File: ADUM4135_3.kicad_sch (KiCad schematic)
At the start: 37 parts, among them Q10 MJD45H11T4G, Q11 MJD44H11T4G, Q12 MJD45H11T4G, Q9 MJD44H11T4G

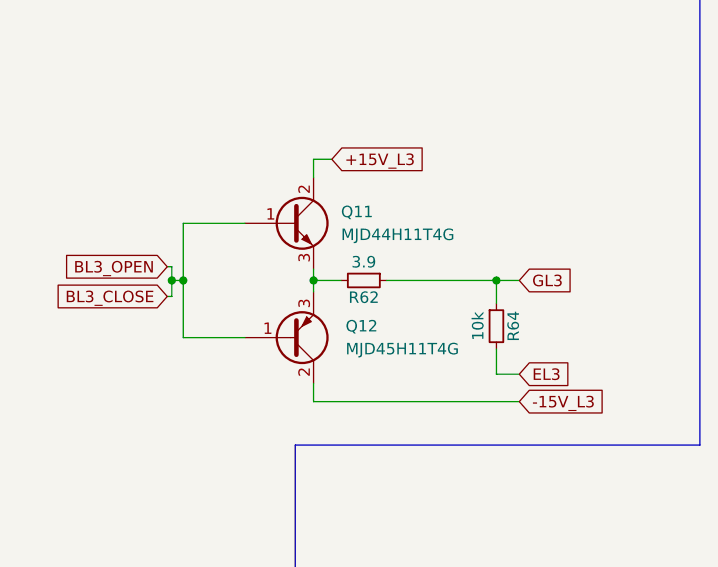
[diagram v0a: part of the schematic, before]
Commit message: REV2.1 - добавил конденсатор по питанию измерения DC
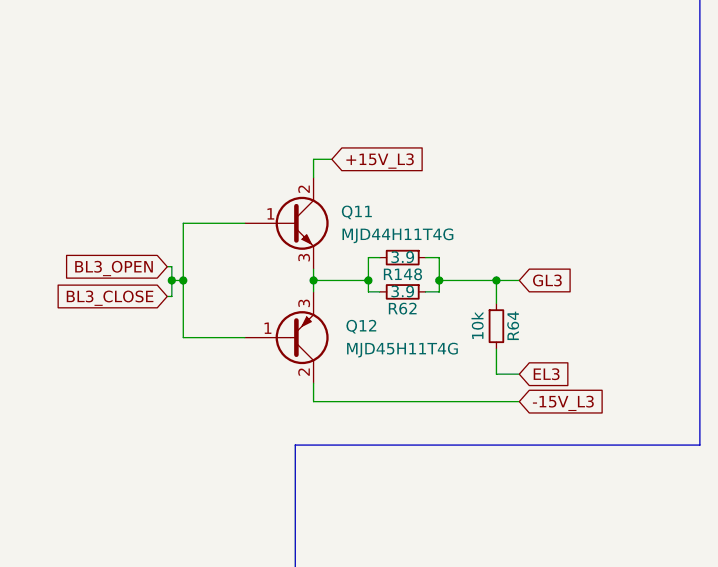
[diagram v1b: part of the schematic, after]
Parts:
- added R148: 3.9, Resistor_SMD:R_2512_6332Metric_Pad1.40x3.35mm_HandSolder, symbol Device:R_Small
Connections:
- net GL3: now also R148.1
- net at Q11.3 (E), Q12.3 (E), R62.2: now also R148.2
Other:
- moved on the sheet: R62
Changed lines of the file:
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@@
   (junction (at 151.892 54.864) (diameter 0) (color 0 0 0 0)
   )
+  (junction (at 173.736 141.478) (diameter 0) (color 0 0 0 0)
+  )
+  (junction (at 179.832 141.478) (diameter 0) (color 0 0 0 0)
+  )
   (junction (at 183.896 54.864) (diameter 0) (color 0 0 0 0)
   )
@@
   (junction (at 126.238 155.448) (diameter 0) (color 0 0 0 0)
   )
-  (junction (at 173.736 141.478) (diameter 0) (color 0 0 0 0)
+  (junction (at 194.056 141.478) (diameter 0) (color 0 0 0 0)
   )
   (junction (at 189.992 54.864) (diameter 0) (color 0 0 0 0)
@@
   (junction (at 117.602 61.722) (diameter 0) (color 0 0 0 0)
   )
-  (junction (at 194.056 141.478) (diameter 0) (color 0 0 0 0)
-  )
   (junction (at 112.522 61.722) (diameter 0) (color 0 0 0 0)
   )
@@
   )
   (junction (at 109.982 155.448) (diameter 0) (color 0 0 0 0)
+  )
+  (junction (at 187.706 141.478) (diameter 0) (color 0 0 0 0)
   )
   (junction (at 167.64 54.864) (diameter 0) (color 0 0 0 0)
@@
     (stroke (width 0) (type default) (color 0 0 0 0))
   )
+  (wire (pts (xy 179.832 138.938) (xy 179.832 141.478))
+    (stroke (width 0) (type default) (color 0 0 0 0))
+  )
   (wire (pts (xy 151.384 53.34) (xy 151.892 53.34))
     (stroke (width 0) (type default) (color 0 0 0 0))
@@
     (stroke (width 0) (type default) (color 0 0 0 0))
   )
-  (wire (pts (xy 173.736 141.478) (xy 176.784 141.478))
-    (stroke (width 0) (type default) (color 0 0 0 0))
-  )
   (wire (pts (xy 177.546 52.578) (xy 176.53 52.578))
     (stroke (width 0) (type default) (color 0 0 0 0))
   )
+  (wire (pts (xy 173.736 141.478) (xy 173.736 142.748))
+    (stroke (width 0) (type default) (color 0 0 0 0))
+  )
   (wire (pts (xy 167.64 53.594) (xy 167.64 54.864))
     (stroke (width 0) (type default) (color 0 0 0 0))
   )
+  (wire (pts (xy 173.736 141.478) (xy 179.832 141.478))
+    (stroke (width 0) (type default) (color 0 0 0 0))
+  )
   (wire (pts (xy 109.982 155.448) (xy 109.982 146.812))
     (stroke (width 0) (type default) (color 0 0 0 0))
@@
     (stroke (width 0) (type default) (color 0 0 0 0))
   )
-  (wire (pts (xy 173.736 141.478) (xy 173.736 142.748))
-    (stroke (width 0) (type default) (color 0 0 0 0))
-  )
   (wire (pts (xy 151.892 53.34) (xy 151.892 54.864))
     (stroke (width 0) (type default) (color 0 0 0 0))
   )
+  (wire (pts (xy 181.102 138.938) (xy 179.832 138.938))
+    (stroke (width 0) (type default) (color 0 0 0 0))
+  )
   (polyline (pts (xy 142.24 104.14) (xy 216.662 104.14))
     (stroke (width 0) (type default) (color 0 0 0 0))
@@
     (stroke (width 0) (type default) (color 0 0 0 0))
   )
-  (wire (pts (xy 181.864 141.478) (xy 194.056 141.478))
-    (stroke (width 0) (type default) (color 0 0 0 0))
-  )
   (wire (pts (xy 123.19 139.954) (xy 125.984 139.954))
     (stroke (width 0) (type default) (color 0 0 0 0))
@@
     (stroke (width 0) (type default) (color 0 0 0 0))
   )
+  (wire (pts (xy 179.832 142.748) (xy 181.102 142.748))
+    (stroke (width 0) (type default) (color 0 0 0 0))
+  )
   (wire (pts (xy 107.442 81.788) (xy 110.236 81.788))
     (stroke (width 0) (type default) (color 0 0 0 0))
@@
     (stroke (width 0) (type default) (color 0 0 0 0))
   )
+  (wire (pts (xy 187.706 138.938) (xy 187.706 141.478))
+    (stroke (width 0) (type default) (color 0 0 0 0))
+  )
   (wire (pts (xy 167.64 66.294) (xy 167.64 68.326))
     (stroke (width 0) (type default) (color 0 0 0 0))
@@
     (stroke (width 0) (type default) (color 0 0 0 0))
   )
+  (wire (pts (xy 187.706 142.748) (xy 186.182 142.748))
+    (stroke (width 0) (type default) (color 0 0 0 0))
+  )
   (wire (pts (xy 94.996 65.532) (xy 99.06 65.532))
     (stroke (width 0) (type default) (color 0 0 0 0))
@@
     (stroke (width 0) (type default) (color 0 0 0 0))
   )
+  (wire (pts (xy 187.706 141.478) (xy 187.706 142.748))
+    (stroke (width 0) (type default) (color 0 0 0 0))
+  )
   (wire (pts (xy 104.394 71.882) (xy 107.442 71.882))
     (stroke (width 0) (type default) (color 0 0 0 0))
@@
     (stroke (width 0) (type default) (color 0 0 0 0))
   )
+  (wire (pts (xy 179.832 141.478) (xy 179.832 142.748))
+    (stroke (width 0) (type default) (color 0 0 0 0))
+  )
   (wire (pts (xy 151.892 56.642) (xy 151.892 54.864))
     (stroke (width 0) (type default) (color 0 0 0 0))
@@
     (stroke (width 0) (type default) (color 0 0 0 0))
   )
+  (wire (pts (xy 187.706 141.478) (xy 194.056 141.478))
+    (stroke (width 0) (type default) (color 0 0 0 0))
+  )
   (wire (pts (xy 183.896 57.404) (xy 183.896 54.864))
     (stroke (width 0) (type default) (color 0 0 0 0))
@@
   )
   (wire (pts (xy 94.742 150.622) (xy 98.806 150.622))
+    (stroke (width 0) (type default) (color 0 0 0 0))
+  )
+  (wire (pts (xy 186.182 138.938) (xy 187.706 138.938))
     (stroke (width 0) (type default) (color 0 0 0 0))
   )
@@
     (pin "2")
   )
-  (symbol (lib_id "Device:R_Small") (at 179.324 141.478 270) (unit 1)
+  (symbol (lib_id "Device:R_Small") (at 183.642 142.748 270) (unit 1)
     (in_bom yes) (on_board yes)
-    (property "Reference" "R62" (id 0) (at 179.324 143.383 90))
-    (property "Value" "3.9" (id 1) (at 179.324 139.446 90))
-    (property "Footprint" "Resistor_SMD:R_2512_6332Metric_Pad1.40x3.35mm_HandSolder" (id 2) (at 179.324 141.478 0)
-      (effects (font (size 1.27 1.27)) hide)
-    )
-    (property "Datasheet" "~" (id 3) (at 179.324 141.478 0)
-      (effects (font (size 1.27 1.27)) hide)
-    )
+    (property "Reference" "R62" (id 0) (at 183.642 144.653 90))
+    (property "Value" "3.9" (id 1) (at 183.642 142.748 90))
+    (property "Footprint" "Resistor_SMD:R_2512_6332Metric_Pad1.40x3.35mm_HandSolder" (id 2) (at 183.642 142.748 0)
+      (effects (font (size 1.27 1.27)) hide)
+    )
+    (property "Datasheet" "~" (id 3) (at 183.642 142.748 0)
+      (effects (font (size 1.27 1.27)) hide)
+    )
+    (pin "1")
+    (pin "2")
+  )
+  (symbol (lib_id "Device:R_Small") (at 183.642 138.938 270) (unit 1)
+    (in_bom yes) (on_board yes)
+    (property "Reference" "R148" (id 0) (at 183.642 140.843 90))
+    (property "Value" "3.9" (id 1) (at 183.642 138.938 90))
+    (property "Footprint" "Resistor_SMD:R_2512_6332Metric_Pad1.40x3.35mm_HandSolder" (id 2) (at 183.642 138.938 0)
+      (effects (font (size 1.27 1.27)) hide)
+    )
+    (property "Datasheet" "~" (id 3) (at 183.642 138.938 0)
+      (effects (font (size 1.27 1.27)) hide)
+    )

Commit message: Версия для резонита REV2.1
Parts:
- removed R58, R60: 2.2k, Resistor_SMD:R_0805_2012Metric_Pad1.20x1.40mm_HandSolder, symbol Device:R_Small
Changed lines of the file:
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@@
   (junction (at 189.992 54.864) (diameter 0) (color 0 0 0 0)
-  )
-  (junction (at 117.602 61.722) (diameter 0) (color 0 0 0 0)
   )
   (junction (at 112.522 61.722) (diameter 0) (color 0 0 0 0)
@@
     (stroke (width 0) (type default) (color 0 0 0 0))
   )
-  (wire (pts (xy 126.238 70.866) (xy 126.238 61.722))
-    (stroke (width 0) (type default) (color 0 0 0 0))
-  )
   (wire (pts (xy 159.258 135.128) (xy 159.258 141.478))
     (stroke (width 0) (type default) (color 0 0 0 0))
@@
     (stroke (width 0) (type default) (color 0 0 0 0))
   )
-  (wire (pts (xy 113.03 139.954) (xy 118.11 139.954))
-    (stroke (width 0) (type default) (color 0 0 0 0))
-  )
   (wire (pts (xy 183.896 54.864) (xy 189.992 54.864))
     (stroke (width 0) (type default) (color 0 0 0 0))
@@
     (stroke (width 0) (type default) (color 0 0 0 0))
   )
-  (wire (pts (xy 123.19 139.954) (xy 125.984 139.954))
-    (stroke (width 0) (type default) (color 0 0 0 0))
-  )
   (wire (pts (xy 151.892 54.864) (xy 153.162 54.864))
     (stroke (width 0) (type default) (color 0 0 0 0))
@@
     (stroke (width 0) (type default) (color 0 0 0 0))
   )
-  (wire (pts (xy 113.03 141.986) (xy 109.982 141.986))
-    (stroke (width 0) (type default) (color 0 0 0 0))
-  )
-  (wire (pts (xy 109.982 141.986) (xy 109.982 146.812))
-    (stroke (width 0) (type default) (color 0 0 0 0))
-  )
   (wire (pts (xy 94.996 57.912) (xy 99.06 57.912))
     (stroke (width 0) (type default) (color 0 0 0 0))
@@
     (stroke (width 0) (type default) (color 0 0 0 0))
   )
-  (wire (pts (xy 126.238 61.722) (xy 117.602 61.722))
-    (stroke (width 0) (type default) (color 0 0 0 0))
-  )
   (polyline (pts (xy 38.1 96.139) (xy 38.1 19.05))
     (stroke (width 0) (type default) (color 0 0 0 0))
@@
     (stroke (width 0) (type default) (color 0 0 0 0))
   )
-  (wire (pts (xy 113.03 141.986) (xy 113.03 139.954))
-    (stroke (width 0) (type default) (color 0 0 0 0))
-  )
   (wire (pts (xy 153.162 48.514) (xy 153.162 54.864))
     (stroke (width 0) (type default) (color 0 0 0 0))
@@
   )
   (wire (pts (xy 70.866 65.532) (xy 68.58 65.532))
-    (stroke (width 0) (type default) (color 0 0 0 0))
-  )
-  (wire (pts (xy 126.238 75.946) (xy 126.238 78.74))
     (stroke (width 0) (type default) (color 0 0 0 0))
   )
@@
     )
   )
-  (global_label "+15V_H3" (shape input) (at 126.238 78.74 270) (fields_autoplaced)
-    (effects (font (size 1.27 1.27)) (justify right))
-    (property "Intersheet References" "${INTERSHEET_REFS}" (id 0) (at 126.1586 89.7407 90)
-      (effects (font (size 1.27 1.27)) (justify right) hide)
-    )
-  )
   (global_label "FLT_L3" (shape input) (at 70.612 139.192 180) (fields_autoplaced)
     (effects (font (size 1.27 1.27)) (justify right))
@@
     (effects (font (size 1.27 1.27)) (justify left))
     (property "Intersheet References" "${INTERSHEET_REFS}" (id 0) (at 113.2539 54.0226 0)
-      (effects (font (size 1.27 1.27)) (justify left) hide)
-    )
-  )
-  (global_label "+15V_L3" (shape input) (at 125.984 139.954 0) (fields_autoplaced)
-    (effects (font (size 1.27 1.27)) (justify left))
-    (property "Intersheet References" "${INTERSHEET_REFS}" (id 0) (at 136.6823 139.8746 0)
       (effects (font (size 1.27 1.27)) (justify left) hide)
     )
@@
     (pin "1")
   )
-  (symbol (lib_id "Device:R_Small") (at 126.238 73.406 0) (unit 1)
-    (in_bom yes) (on_board yes)
-    (property "Reference" "R60" (id 0) (at 128.27 73.406 0))
-    (property "Value" "2.2k" (id 1) (at 124.206 73.406 90))
-    (property "Footprint" "Resistor_SMD:R_0805_2012Metric_Pad1.20x1.40mm_HandSolder" (id 2) (at 126.238 73.406 0)
-      (effects (font (size 1.27 1.27)) hide)
-    )
-    (property "Datasheet" "~" (id 3) (at 126.238 73.406 0)
-      (effects (font (size 1.27 1.27)) hide)
-    )
-    (pin "1")
-    (pin "2")
-  )
   (symbol (lib_id "power:GND") (at 57.15 153.162 0) (unit 1)
     (in_bom yes) (on_board yes)
@@
     (pin "1")
   )
-  (symbol (lib_id "Device:R_Small") (at 120.65 139.954 90) (unit 1)
-    (in_bom yes) (on_board yes)
-    (property "Reference" "R58" (id 0) (at 120.65 137.922 90))
-    (property "Value" "2.2k" (id 1) (at 120.65 141.986 90))
-    (property "Footprint" "Resistor_SMD:R_0805_2012Metric_Pad1.20x1.40mm_HandSolder" (id 2) (at 120.65 139.954 0)
-      (effects (font (size 1.27 1.27)) hide)
-    )
-    (property "Datasheet" "~" (id 3) (at 120.65 139.954 0)
-      (effects (font (size 1.27 1.27)) hide)
-    )
-    (pin "1")
-    (pin "2")
-  )
   (symbol (lib_id "Device:R_Small") (at 180.086 52.578 270) (unit 1)

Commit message: Финальная версия для производства
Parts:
- R145, R148, R61, R62: value 3.9 -> 3
- R51, R52, R53, R54: value 3.9 -> 50
- R57, R59: value 0 -> 10k
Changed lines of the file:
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@@
     (in_bom yes) (on_board yes)
     (property "Reference" "R61" (id 0) (at 180.086 54.483 90))
-    (property "Value" "3.9" (id 1) (at 180.086 52.578 90))
+    (property "Value" "3" (id 1) (at 180.086 52.578 90))
     (property "Footprint" "Resistor_SMD:R_2512_6332Metric_Pad1.40x3.35mm_HandSolder" (id 2) (at 180.086 52.578 0)
       (effects (font (size 1.27 1.27)) hide)
@@
     (in_bom yes) (on_board yes)
     (property "Reference" "R62" (id 0) (at 183.642 144.653 90))
-    (property "Value" "3.9" (id 1) (at 183.642 142.748 90))
+    (property "Value" "3" (id 1) (at 183.642 142.748 90))
     (property "Footprint" "Resistor_SMD:R_2512_6332Metric_Pad1.40x3.35mm_HandSolder" (id 2) (at 183.642 142.748 0)
       (effects (font (size 1.27 1.27)) hide)
@@
     (in_bom yes) (on_board yes)
     (property "Reference" "R148" (id 0) (at 183.642 140.843 90))
-    (property "Value" "3.9" (id 1) (at 183.642 138.938 90))
+    (property "Value" "3" (id 1) (at 183.642 138.938 90))
     (property "Footprint" "Resistor_SMD:R_2512_6332Metric_Pad1.40x3.35mm_HandSolder" (id 2) (at 183.642 138.938 0)
       (effects (font (size 1.27 1.27)) hide)
@@
     (in_bom yes) (on_board yes)
     (property "Reference" "R59" (id 0) (at 120.65 144.526 90))
-    (property "Value" "0" (id 1) (at 120.65 149.352 90))
+    (property "Value" "10k" (id 1) (at 120.65 149.352 90))
     (property "Footprint" "Resistor_SMD:R_1206_3216Metric_Pad1.30x1.75mm_HandSolder" (id 2) (at 120.65 146.812 0)
       (effects (font (size 1.27 1.27)) hide)
@@
     (in_bom yes) (on_board yes)
     (property "Reference" "R54" (id 0) (at 97.536 56.007 90))
-    (property "Value" "3.9" (id 1) (at 97.536 52.07 90))
+    (property "Value" "50" (id 1) (at 97.536 52.07 90))
     (property "Footprint" "Resistor_SMD:R_1210_3225Metric_Pad1.30x2.65mm_HandSolder" (id 2) (at 97.536 54.102 0)
       (effects (font (size 1.27 1.27)) hide)
@@
     (in_bom yes) (on_board yes)
     (property "Reference" "R145" (id 0) (at 180.086 59.309 90))
-    (property "Value" "3.9" (id 1) (at 180.086 57.404 90))
+    (property "Value" "3" (id 1) (at 180.086 57.404 90))
     (property "Footprint" "Resistor_SMD:R_2512_6332Metric_Pad1.40x3.35mm_HandSolder" (id 2) (at 180.086 57.404 0)
       (effects (font (size 1.27 1.27)) hide)
@@
     (in_bom yes) (on_board yes)
     (property "Reference" "D28" (id 0) (at 126.238 144.526 0))
-    (property "Value" "MURS360T3G" (id 1) (at 127 149.352 0))
+    (property "Value" "MURS360T3G" (id 1) (at 129.54 149.352 0))
     (property "Footprint" "Diode_SMD:D_SMC" (id 2) (at 126.238 146.812 90)
       (effects (font (size 1.27 1.27)) hide)
@@
     (in_bom yes) (on_board yes)
     (property "Reference" "R57" (id 0) (at 119.888 73.406 0))
-    (property "Value" "0" (id 1) (at 115.57 73.406 90))
+    (property "Value" "10k" (id 1) (at 115.57 73.406 90))
     (property "Footprint" "Resistor_SMD:R_1206_3216Metric_Pad1.30x1.75mm_HandSolder" (id 2) (at 117.602 73.406 0)
       (effects (font (size 1.27 1.27)) hide)
@@
     (in_bom yes) (on_board yes)
     (property "Reference" "R51" (id 0) (at 97.282 133.477 90))
-    (property "Value" "3.9" (id 1) (at 97.282 129.54 90))
+    (property "Value" "50" (id 1) (at 97.282 129.54 90))
     (property "Footprint" "Resistor_SMD:R_1210_3225Metric_Pad1.30x2.65mm_HandSolder" (id 2) (at 97.282 131.572 0)
       (effects (font (size 1.27 1.27)) hide)
@@
     (in_bom yes) (on_board yes)
     (property "Reference" "R52" (id 0) (at 97.282 141.097 90))
-    (property "Value" "3.9" (id 1) (at 97.282 137.16 90))
+    (property "Value" "50" (id 1) (at 97.282 137.16 90))
     (property "Footprint" "Resistor_SMD:R_1210_3225Metric_Pad1.30x2.65mm_HandSolder" (id 2) (at 97.282 139.192 0)
       (effects (font (size 1.27 1.27)) hide)
@@
     (in_bom yes) (on_board yes)
     (property "Reference" "R53" (id 0) (at 97.536 48.387 90))
-    (property "Value" "3.9" (id 1) (at 97.536 44.45 90))
+    (property "Value" "50" (id 1) (at 97.536 44.45 90))
     (property "Footprint" "Resistor_SMD:R_1210_3225Metric_Pad1.30x2.65mm_HandSolder" (id 2) (at 97.536 46.482 0)
       (effects (font (size 1.27 1.27)) hide)
